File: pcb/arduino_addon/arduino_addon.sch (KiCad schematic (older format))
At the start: 32 parts, among them P1 AnalogIn, P11 ADC-DO, P12 ADC-DO, P13 ADC-DO, P14 ADC-DO, P15 DO, P16 3V3 ADC REF, P2 Power, P3 Digital1, P4 Digital2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

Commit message: arduino addon board pcb design is ready
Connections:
- net labels removed: +3V3, ADC0, ADC3
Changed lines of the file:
@@
 $EndComp
 $Comp
-L +5V #PWR010
-U 1 1 5834301B
-P 4800 800
-F 0 "#PWR010" H 4800 650 50  0001 C CNN
-F 1 "+3V3" H 4800 940 50  0000 C CNN
-F 2 "" H 4800 800 50  0000 C CNN
-F 3 "" H 4800 800 50  0000 C CNN
-	1    4800 800
-	1    0    0    -1
-$EndComp
-$Comp
-L GND #PWR011
+L GND #PWR010
 U 1 1 583430C0
 P 4800 1650
-F 0 "#PWR011" H 4800 1400 50  0001 C CNN
+F 0 "#PWR010" H 4800 1400 50  0001 C CNN
 F 1 "GND" H 4800 1500 50  0000 C CNN
 F 2 "" H 4800 1650 50  0000 C CNN
@@
 $EndComp
 $Comp
-L GND #PWR015
+L GND #PWR011
 U 1 1 58345774
 P 1250 7550
-F 0 "#PWR015" H 1250 7300 50  0001 C CNN
+F 0 "#PWR011" H 1250 7300 50  0001 C CNN
 F 1 "GND" H 1250 7400 50  0000 C CNN
 F 2 "" H 1250 7550 50  0000 C CNN
@@
 $EndComp
 $Comp
-L GND #PWR016
+L GND #PWR012
 U 1 1 583459DE
 P 1650 7550
-F 0 "#PWR016" H 1650 7300 50  0001 C CNN
+F 0 "#PWR012" H 1650 7300 50  0001 C CNN
 F 1 "GND" H 1650 7400 50  0000 C CNN
 F 2 "" H 1650 7550 50  0000 C CNN
@@
 $EndComp
 $Comp
-L GND #PWR017
+L GND #PWR013
 U 1 1 583482C3
 P 4900 3000
-F 0 "#PWR017" H 4900 2750 50  0001 C CNN
+F 0 "#PWR013" H 4900 2750 50  0001 C CNN
 F 1 "GND" H 4900 2850 50  0000 C CNN
 F 2 "" H 4900 3000 50  0000 C CNN
 F 3 "" H 4900 3000 50  0000 C CNN
 	1    4900 3000
-	1    0    0    -1
-$EndComp
-$Comp
-L +5V #PWR018
-U 1 1 583484A5
-P 4900 2250
-F 0 "#PWR018" H 4900 2100 50  0001 C CNN
-F 1 "+3V3" H 4900 2390 50  0000 C CNN
-F 2 "" H 4900 2250 50  0000 C CNN
-F 3 "" H 4900 2250 50  0000 C CNN
-	1    4900 2250
 	1    0    0    -1
 $EndComp
@@
 $EndComp
 $Comp
-L GND #PWR019
+L GND #PWR014
 U 1 1 58348E19
 P 4900 4350
-F 0 "#PWR019" H 4900 4100 50  0001 C CNN
+F 0 "#PWR014" H 4900 4100 50  0001 C CNN
 F 1 "GND" H 4900 4200 50  0000 C CNN
 F 2 "" H 4900 4350 50  0000 C CNN
 F 3 "" H 4900 4350 50  0000 C CNN
 	1    4900 4350
-	1    0    0    -1
-$EndComp
-$Comp
-L +5V #PWR020
-U 1 1 58348E1F
-P 4900 3600
-F 0 "#PWR020" H 4900 3450 50  0001 C CNN
-F 1 "+3V3" H 4900 3740 50  0000 C CNN
-F 2 "" H 4900 3600 50  0000 C CNN
-F 3 "" H 4900 3600 50  0000 C CNN
-	1    4900 3600
 	1    0    0    -1
 $EndComp
@@
 $EndComp
 $Comp
-L GND #PWR021
+L GND #PWR015
 U 1 1 58349814
 P 4900 5900
-F 0 "#PWR021" H 4900 5650 50  0001 C CNN
+F 0 "#PWR015" H 4900 5650 50  0001 C CNN
 F 1 "GND" H 4900 5750 50  0000 C CNN
 F 2 "" H 4900 5900 50  0000 C CNN
 F 3 "" H 4900 5900 50  0000 C CNN
 	1    4900 5900
-	1    0    0    -1
-$EndComp
-$Comp
-L +5V #PWR022
-U 1 1 5834981A
-P 4900 5150
-F 0 "#PWR022" H 4900 5000 50  0001 C CNN
-F 1 "+3V3" H 4900 5290 50  0000 C CNN
-F 2 "" H 4900 5150 50  0000 C CNN
-F 3 "" H 4900 5150 50  0000 C CNN
-	1    4900 5150
 	1    0    0    -1
 $EndComp
@@
 $EndComp
 $Comp
-L GND #PWR023
+L GND #PWR016
 U 1 1 5834982D
 P 4900 7250
-F 0 "#PWR023" H 4900 7000 50  0001 C CNN
+F 0 "#PWR016" H 4900 7000 50  0001 C CNN
 F 1 "GND" H 4900 7100 50  0000 C CNN
 F 2 "" H 4900 7250 50  0000 C CNN
 F 3 "" H 4900 7250 50  0000 C CNN
 	1    4900 7250
-	1    0    0    -1
-$EndComp
-$Comp
-L +5V #PWR024
-U 1 1 58349833
-P 4900 6500
-F 0 "#PWR024" H 4900 6350 50  0001 C CNN
-F 1 "+3V3" H 4900 6640 50  0000 C CNN
-F 2 "" H 4900 6500 50  0000 C CNN
-F 3 "" H 4900 6500 50  0000 C CNN
-	1    4900 6500
 	1    0    0    -1
 $EndComp
@@
 DAC0
 Text Label 6150 2950 2    60   ~ 0
-ADC3
+AI3
 $Comp
 L CONN_01X03 P11
@@
 $EndComp
 $Comp
-L GND #PWR025
+L GND #PWR017
 U 1 1 58350536
 P 7400 3500
-F 0 "#PWR025" H 7400 3250 50  0001 C CNN
+F 0 "#PWR017" H 7400 3250 50  0001 C CNN
 F 1 "GND" H 7400 3350 50  0000 C CNN
 F 2 "" H 7400 3500 50  0000 C CNN
@@
 	6500 1950 6500 2050
 $Comp
-L GND #PWR026
+L GND #PWR018
 U 1 1 58358BCB
 P 6500 2050
-F 0 "#PWR026" H 6500 1800 50  0001 C CNN
+F 0 "#PWR018" H 6500 1800 50  0001 C CNN
 F 1 "GND" H 6500 1900 50  0000 C CNN
 F 2 "" H 6500 2050 50  0000 C CNN
@@
 	7050 1800 7050 1950
 $Comp
-L GND #PWR027
+L GND #PWR019
 U 1 1 58358CEF
 P 7050 1950
-F 0 "#PWR027" H 7050 1700 50  0001 C CNN
+F 0 "#PWR019" H 7050 1700 50  0001 C CNN
 F 1 "GND" H 7050 1800 50  0000 C CNN
 F 2 "" H 7050 1950 50  0000 C CNN
@@
 	6200 1400 6200 1600
 $Comp
-L GND #PWR028
+L GND #PWR020
 U 1 1 58359BA6
 P 6200 1600
-F 0 "#PWR028" H 6200 1350 50  0001 C CNN
+F 0 "#PWR020" H 6200 1350 50  0001 C CNN
 F 1 "GND" H 6200 1450 50  0000 C CNN
 F 2 "" H 6200 1600 50  0000 C CNN
@@
 Wire Wire Line
 	7050 1200 7050 950
-$Comp
-L +5V #PWR029
-U 1 1 58359D1F
-P 7050 950
-F 0 "#PWR029" H 7050 800 50  0001 C CNN
-F 1 "+3V3" H 7050 1090 50  0000 C CNN
-F 2 "" H 7050 950 50  0000 C CNN
-F 3 "" H 7050 950 50  0000 C CNN
-	1    7050 950
-	1    0    0    -1
-$EndComp
 $Comp
 L LM324 U1
@@
 $EndComp
 $Comp
-L GND #PWR031
+L GND #PWR021
 U 1 1 5838D934
 P 2600 6750
-F 0 "#PWR031" H 2600 6500 50  0001 C CNN
+F 0 "#PWR021" H 2600 6500 50  0001 C CNN
 F 1 "GND" H 2600 6600 50  0000 C CNN
 F 2 "" H 2600 6750 50  0000 C CNN
@@
 $EndComp
 $Comp
-L GND #PWR032
+L GND #PWR022
 U 1 1 5838D93A
 P 3200 6600
-F 0 "#PWR032" H 3200 6350 50  0001 C CNN
+F 0 "#PWR022" H 3200 6350 50  0001 C CNN
 F 1 "GND" H 3200 6450 50  0000 C CNN
 F 2 "" H 3200 6600 50  0000 C CNN
 F 3 "" H 3200 6600 50  0000 C CNN
 	1    3200 6600
-	1    0    0    -1
-$EndComp
-$Comp
-L +5V #PWR033
-U 1 1 5838D940
-P 3200 5900
-F 0 "#PWR033" H 3200 5750 50  0001 C CNN
-F 1 "+3V3" H 3200 6040 50  0000 C CNN
-F 2 "" H 3200 5900 50  0000 C CNN
-F 3 "" H 3200 5900 50  0000 C CNN
-	1    3200 5900
 	1    0    0    -1
 $EndComp
@@
 	2800 7150 2800 7250
 $Comp
-L GND #PWR034
+L GND #PWR023
 U 1 1 5838D963
 P 2800 7250
-F 0 "#PWR034" H 2800 7000 50  0001 C CNN
+F 0 "#PWR023" H 2800 7000 50  0001 C CNN
 F 1 "GND" H 2800 7100 50  0000 C CNN
 F 2 "" H 2800 7250 50  0000 C CNN
@@
 	1950 6150 2250 6150
 $Comp
-L +3V3 #PWR035
-U 1 1 5839123E
-P 850 6400
-F 0 "#PWR035" H 850 6250 50  0001 C CNN
-F 1 "+3V3" H 850 6540 50  0000 C CNN
-F 2 "" H 850 6400 50  0000 C CNN
-F 3 "" H 850 6400 50  0000 C CNN
-	1    850  6400
-	1    0    0    -1
-$EndComp
-$Comp
 L CONN_01X02 P16
 U 1 1 58394226
@@
 	7500 2750 7100 2750
 Text Label 7300 2750 2    60   ~ 0
-ADC0
+AD0
 Wire Wire Line
 	7500 2650 7400 2650
 Wire Wire Line
 	7400 2650 7400 2600
-$Comp
-L +3V3 #PWR036
-U 1 1 583944B9
+Wire Wire Line
+	1100 4350 1950 4350
+Wire Wire Line
+	1950 4350 1950 6150
+Wire Wire Line
+	1100 4250 1700 4250
+$Comp
+L +3.3V #PWR024
+U 1 1 583C1430
+P 7050 950
+F 0 "#PWR024" H 7050 800 50  0001 C CNN
+F 1 "+3.3V" H 7050 1090 50  0000 C CNN
+F 2 "" H 7050 950 50  0000 C CNN
+F 3 "" H 7050 950 50  0000 C CNN
+	1    7050 950
+	1    0    0    -1
+$EndComp
+$Comp
+L +3.3V #PWR025
+U 1 1 583C15D0
+P 4900 2250
+F 0 "#PWR025" H 4900 2100 50  0001 C CNN
+F 1 "+3.3V" H 4900 2390 50  0000 C CNN
+F 2 "" H 4900 2250 50  0000 C CNN
+F 3 "" H 4900 2250 50  0000 C CNN
+	1    4900 2250
+	1    0    0    -1
+$EndComp
+$Comp
+L +3.3V #PWR026
+U 1 1 583C1770
+P 4900 3600
+F 0 "#PWR026" H 4900 3450 50  0001 C CNN
+F 1 "+3.3V" H 4900 3740 50  0000 C CNN
+F 2 "" H 4900 3600 50  0000 C CNN
+F 3 "" H 4900 3600 50  0000 C CNN
+	1    4900 3600
+	1    0    0    -1
+$EndComp
+$Comp
+L +3.3V #PWR027
+U 1 1 583C18C8
+P 4900 5150
+F 0 "#PWR027" H 4900 5000 50  0001 C CNN
+F 1 "+3.3V" H 4900 5290 50  0000 C CNN
+F 2 "" H 4900 5150 50  0000 C CNN
+F 3 "" H 4900 5150 50  0000 C CNN
+	1    4900 5150
+	1    0    0    -1
+$EndComp
+$Comp
+L +3.3V #PWR028
+U 1 1 583C1924
+P 4900 6500
+F 0 "#PWR028" H 4900 6350 50  0001 C CNN
+F 1 "+3.3V" H 4900 6640 50  0000 C CNN
+F 2 "" H 4900 6500 50  0000 C CNN
+F 3 "" H 4900 6500 50  0000 C CNN
+	1    4900 6500
+	1    0    0    -1
+$EndComp
+$Comp
+L +3.3V #PWR029
+U 1 1 583C19C8
+P 3200 5900
+F 0 "#PWR029" H 3200 5750 50  0001 C CNN
+F 1 "+3.3V" H 3200 6040 50  0000 C CNN
+F 2 "" H 3200 5900 50  0000 C CNN
+F 3 "" H 3200 5900 50  0000 C CNN
+	1    3200 5900
+	1    0    0    -1
+$EndComp
+$Comp
+L +3.3V #PWR030
+U 1 1 583C1C66
+P 4800 800
+F 0 "#PWR030" H 4800 650 50  0001 C CNN
+F 1 "+3.3V" H 4800 940 50  0000 C CNN
+F 2 "" H 4800 800 50  0000 C CNN
+F 3 "" H 4800 800 50  0000 C CNN
+	1    4800 800
+	1    0    0    -1
+$EndComp
+$Comp
+L +3.3V #PWR031
+U 1 1 583C1D76
 P 7400 2600
-F 0 "#PWR036" H 7400 2450 50  0001 C CNN
-F 1 "+3V3" H 7400 2740 50  0000 C CNN
+F 0 "#PWR031" H 7400 2450 50  0001 C CNN
+F 1 "+3.3V" H 7400 2740 50  0000 C CNN
 F 2 "" H 7400 2600 50  0000 C CNN
 F 3 "" H 7400 2600 50  0000 C CNN
@@
 	1    0    0    -1
 $EndComp
-Wire Wire Line
-	1100 4350 1950 4350
-Wire Wire Line
-	1950 4350 1950 6150
-Wire Wire Line
-	1100 4250 1700 4250
+$Comp
+L +3.3V #PWR032
+U 1 1 583C1E87
+P 850 6400
+F 0 "#PWR032" H 850 6250 50  0001 C CNN
+F 1 "+3.3V" H 850 6540 50  0000 C CNN
+F 2 "" H 850 6400 50  0000 C CNN
+F 3 "" H 850 6400 50  0000 C CNN
+	1    850  6400
+	1    0    0    -1
+$EndComp
 $EndSCHEMATC

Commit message: bom and pdf files are generated
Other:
- note removed: "TODOS:\n DAC output to adc OK\n light sensor amplifier OK\n lowpass parameters 3.9 k, 0.1uF?\n D0-D7 header? OK"
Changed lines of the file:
@@
 Text Notes 2200 850  2    60   ~ 0
 temp sensor
-Text Notes 7700 5600 2    60   ~ 0
-TODOS:\n DAC output to adc OK\n light sensor amplifier OK\n lowpass parameters 3.9 k, 0.1uF?\n D0-D7 header? OK
 $Comp
 L CONN_01X02 P9

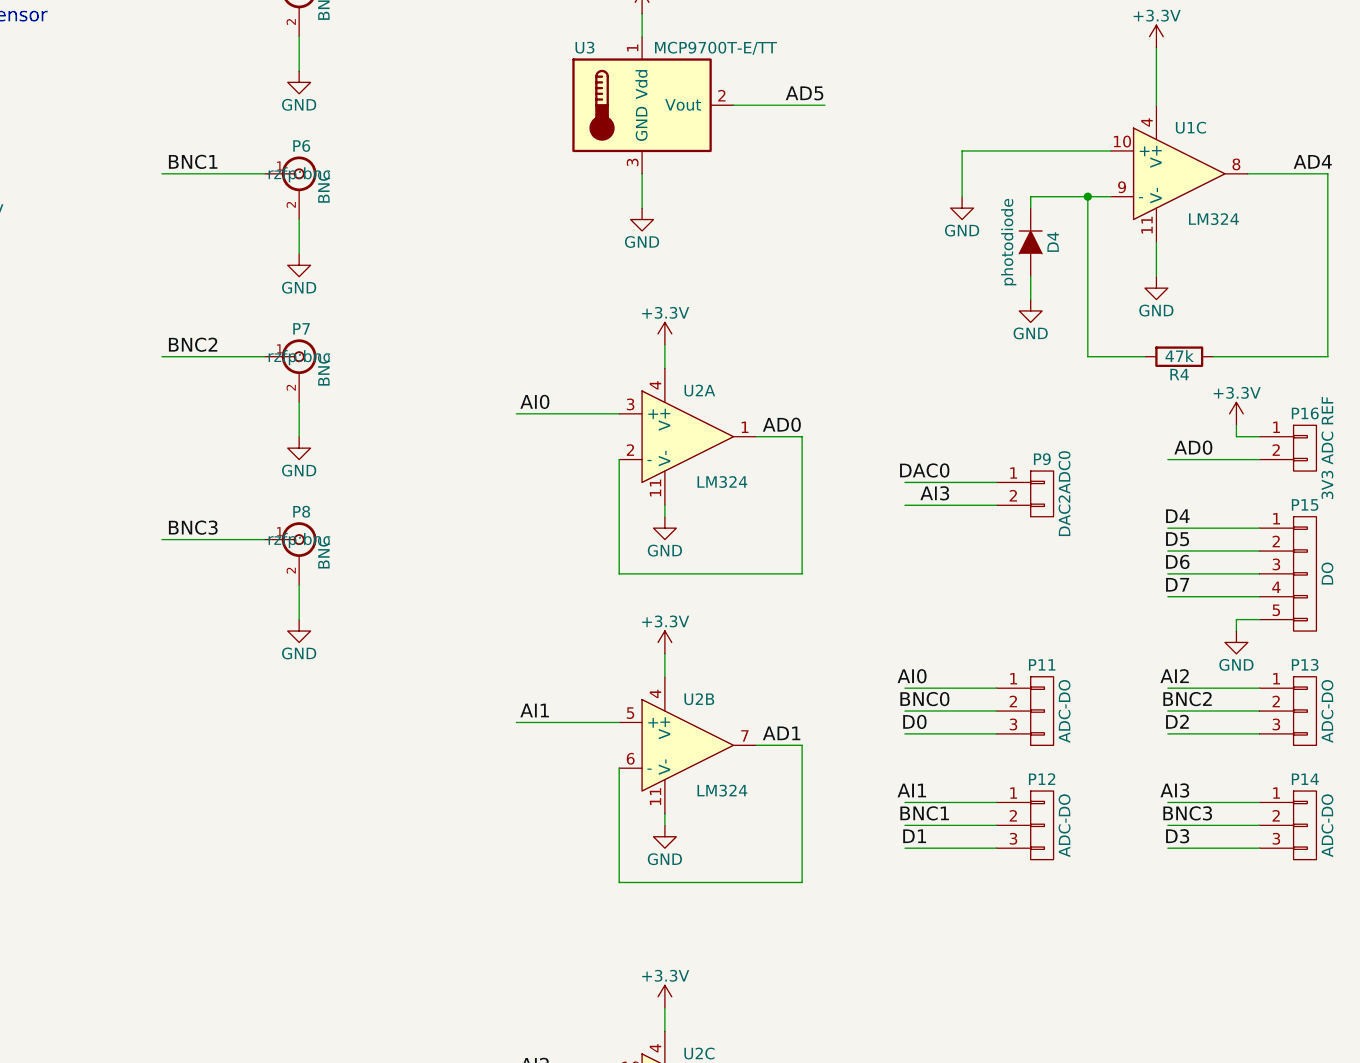
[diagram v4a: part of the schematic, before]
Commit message: adaq initial version, board design: extra bnc connector added
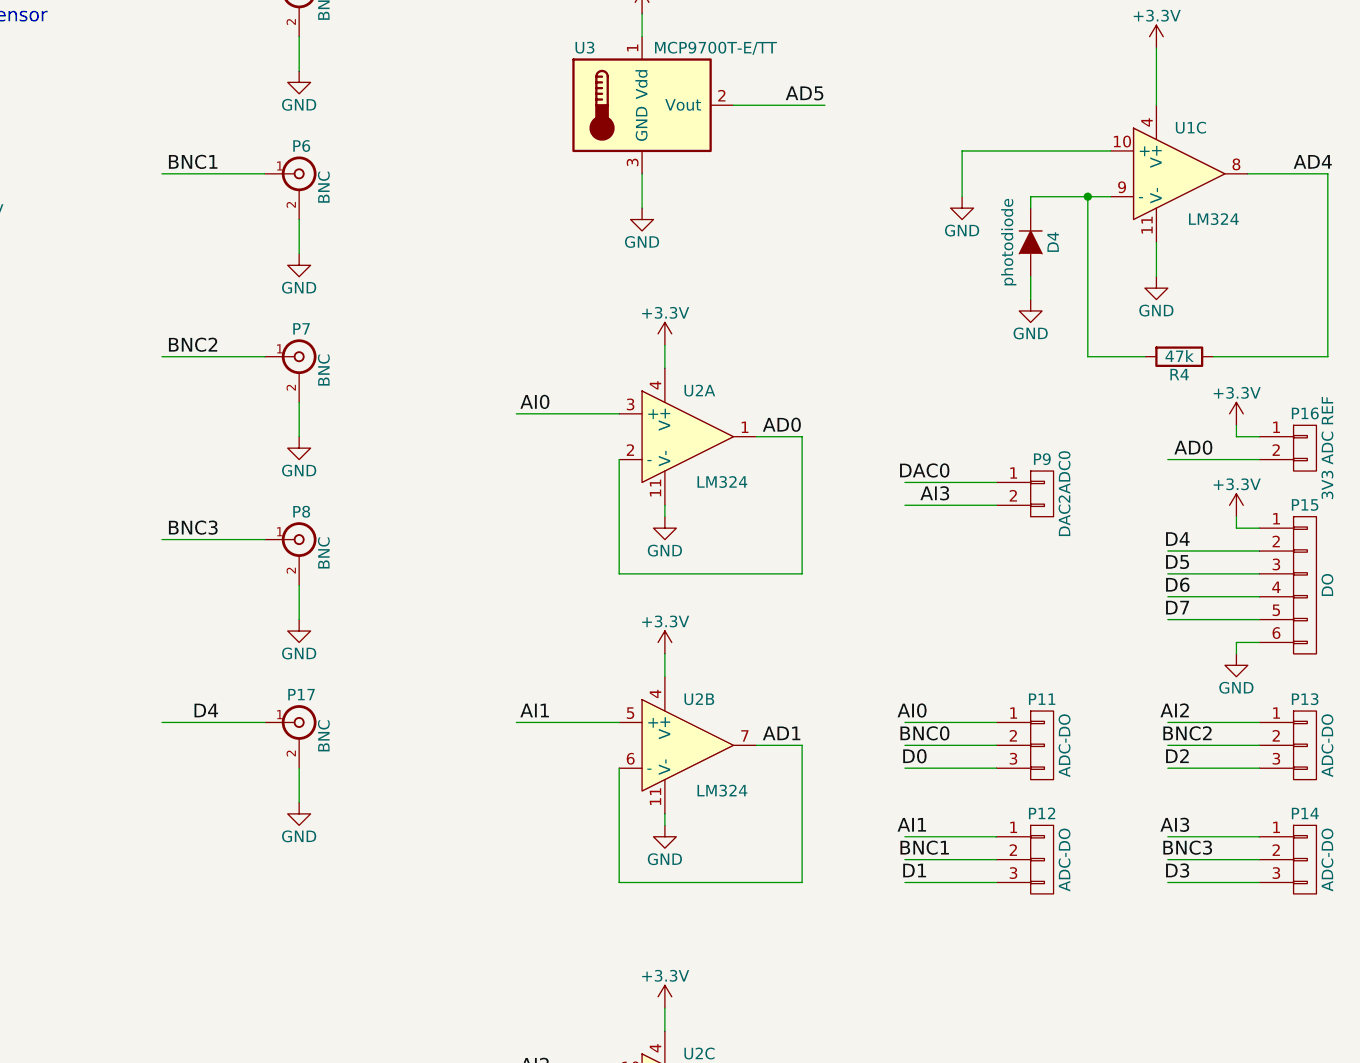
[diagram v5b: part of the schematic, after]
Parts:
- removed P15: DO, Pin_Headers:Pin_Header_Straight_1x05, symbol CONN_01X05
- added P15: DO, Pin_Headers:Pin_Header_Straight_1x06, symbol CONN_01X06
- added P17: BNC, rzfp:bnc, symbol BNC
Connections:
- wire segments 129 -> 133
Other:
- moved on the sheet: P11, P12, P13, P14
